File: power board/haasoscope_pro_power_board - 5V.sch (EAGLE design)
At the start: 123 parts, among them CN1 12Vin, IC11 TPS7A7200RGTR, IC12 TPS7A7200RGTR, IC14 TPS7A7200RGTR, IC3 TPS7A7200RGTR, IC5 TPS72325DBVR, IC7 TPS7A7200RGTR, IC9 TPS7A7200RGTR, J1 2p-2.54, J10 2p-2.54, J11 2p-2.54, J12 2p-2.54, J13 2p-2.54, J14 2p-2.54, J15 2p-2.54, J16 8pin, J17 2p-2.54, J18 2p-2.54, J19 2p-2.54, J2 2p-2.54, J20 2p-2.54, J3 2p-2.54, J4 2p-2.54, J5 2p-2.54, J6 2p-2.54, J7 2p-2.54, J8 2p-2.54, J9 2p-2.54

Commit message: add diode
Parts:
- added D6: B340A, SparkFun-DiscreteSemi:DIODE-SCHOTTKY-B340A
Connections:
- net 2V8-: now also D6.A
- net GND: now also D6.C
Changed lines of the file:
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@@
 <part name="R1" library="FlashPCB_Resistors" deviceset="RES-0402" device="" value="3.3k"/>
 <part name="C4" library="Nordic_nRF" library_urn="urn:adsk.eagle:library:169009" deviceset="CAPACITOR" device="_0805_N" package3d_urn="urn:adsk.eagle:package:2593736/1" value="10uF"/>
+<part name="D6" library="SparkFun-DiscreteSemi" library_urn="urn:adsk.eagle:library:514" deviceset="DIODE-SCHOTTKY" device="-B340A" package3d_urn="urn:adsk.eagle:package:38443/1" value="B340A">
+<attribute name="LCSC" value="C64982"/>
+</part>
 </parts>
 <sheets>
@@
 <attribute name="VALUE" x="90.424" y="-44.831" size="1.778" layer="96"/>
 </instance>
+<instance part="D6" gate="G$1" x="215.9" y="-33.02" smashed="yes" rot="R90">
+<attribute name="NAME" x="213.868" y="-35.56" size="1.778" layer="95" font="vector" rot="R90"/>
+<attribute name="VALUE" x="217.932" y="-35.56" size="1.778" layer="96" font="vector" rot="R90" align="top-left"/>
+<attribute name="LCSC" x="215.9" y="-33.02" size="1.778" layer="96" rot="R90" display="off"/>
+</instance>
 </instances>
 <busses>
@@
 <pinref part="C4" gate="C$1" pin="2"/>
 <wire x1="88.9" y1="-45.72" x2="96.52" y2="-45.72" width="0.1524" layer="91"/>
-<wire x1="109.22" y1="-45.72" x2="109.22" y2="-50.8" width="0.1524" layer="91"/>
-<wire x1="109.22" y1="-50.8" x2="99.06" y2="-50.8" width="0.1524" layer="91"/>
+<wire x1="109.22" y1="-45.72" x2="109.22" y2="-55.88" width="0.1524" layer="91"/>
 <junction x="109.22" y="-45.72"/>
-<label x="99.06" y="-50.8" size="1.778" layer="95"/>
-</segment>
-<segment>
 <pinref part="C55" gate="C$1" pin="2"/>
 <pinref part="R20" gate="G$1" pin="P$1"/>
@@
 <wire x1="144.78" y1="-53.34" x2="154.94" y2="-53.34" width="0.1524" layer="91"/>
 <label x="134.62" y="-55.88" size="1.778" layer="95"/>
+<wire x1="109.22" y1="-55.88" x2="129.54" y2="-55.88" width="0.1524" layer="91"/>
+<junction x="129.54" y="-55.88"/>
 </segment>
 <segment>
@@
 <wire x1="175.26" y1="-38.1" x2="185.42" y2="-38.1" width="0.1524" layer="91"/>
 <label x="195.58" y="-38.1" size="1.778" layer="95"/>
+<pinref part="D6" gate="G$1" pin="A"/>
+<wire x1="200.66" y1="-35.56" x2="215.9" y2="-35.56" width="0.1524" layer="91"/>
+<junction x="200.66" y="-35.56"/>
 </segment>
 </net>
@@
 <junction x="96.52" y="7.62"/>
 <pinref part="GND30" gate="1" pin="GND"/>
-</segment>
-<segment>
+<wire x1="109.22" y1="7.62" x2="109.22" y2="-2.54" width="0.1524" layer="91"/>
+<junction x="109.22" y="7.62"/>
 <pinref part="C41" gate="C$1" pin="2"/>
 <pinref part="R13" gate="G$1" pin="P$1"/>
@@
 <wire x1="144.78" y1="0" x2="154.94" y2="0" width="0.1524" layer="91"/>
 <pinref part="GND31" gate="1" pin="GND"/>
+<wire x1="109.22" y1="-2.54" x2="129.54" y2="-2.54" width="0.1524" layer="91"/>
+<junction x="129.54" y="-2.54"/>
 </segment>
 <segment>
@@
 <junction x="185.42" y="-30.48"/>
 <label x="195.58" y="-30.48" size="1.778" layer="95"/>
+<pinref part="D6" gate="G$1" pin="C"/>
+<wire x1="200.66" y1="-30.48" x2="215.9" y2="-30.48" width="0.1524" layer="91"/>
+<junction x="200.66" y="-30.48"/>
 </segment>
 </net>

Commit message: use more standard resistor values
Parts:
- added R2: 15k, FlashPCB_Resistors:RES-0402
- C48: LCSC (none) -> C307331
- R11, R13, R20: value 55k -> 56k
- R16: value 25k -> 10k
- R25: value 37k -> 39k
- R7: value 71k -> 68k
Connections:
- new net N$14: R16.P$1, R2.P$2
- net GND: now also R2.P$1; no longer R16.P$1
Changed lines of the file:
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@@
 <part name="J14" library="Seeed-Connector" library_urn="urn:adsk.eagle:library:478" deviceset="DIP-BLACK-MALE-HEADER-VERT(2P-2.54)" device="" package3d_urn="urn:adsk.eagle:package:33132/1" value="2p-2.54"/>
 <part name="R23" library="FlashPCB_Resistors" deviceset="RES-0402" device="" value="100k"/>
-<part name="R25" library="FlashPCB_Resistors" deviceset="RES-0402" device="" value="37k"/>
+<part name="R25" library="FlashPCB_Resistors" deviceset="RES-0402" device="" value="39k"/>
 <part name="GND23" library="SparkFun-PowerSymbols" library_urn="urn:adsk.eagle:library:530" deviceset="GND" device=""/>
 <part name="PS3" library="LMR33630ADDA" deviceset="LMR33630ADDA" device=""/>
@@
 <part name="J5" library="Seeed-Connector" library_urn="urn:adsk.eagle:library:478" deviceset="DIP-BLACK-MALE-HEADER-VERT(2P-2.54)" device="" package3d_urn="urn:adsk.eagle:package:33132/1" value="2p-2.54"/>
 <part name="R6" library="FlashPCB_Resistors" deviceset="RES-0402" device="" value="100k"/>
-<part name="R7" library="FlashPCB_Resistors" deviceset="RES-0402" device="" value="71k"/>
+<part name="R7" library="FlashPCB_Resistors" deviceset="RES-0402" device="" value="68k"/>
 <part name="GND26" library="SparkFun-PowerSymbols" library_urn="urn:adsk.eagle:library:530" deviceset="GND" device=""/>
 <part name="PS5" library="LMR33630ADDA" deviceset="LMR33630ADDA" device=""/>
@@
 <part name="J7" library="Seeed-Connector" library_urn="urn:adsk.eagle:library:478" deviceset="DIP-BLACK-MALE-HEADER-VERT(2P-2.54)" device="" package3d_urn="urn:adsk.eagle:package:33132/1" value="2p-2.54"/>
 <part name="R8" library="FlashPCB_Resistors" deviceset="RES-0402" device="" value="100k"/>
-<part name="R11" library="FlashPCB_Resistors" deviceset="RES-0402" device="" value="55k"/>
+<part name="R11" library="FlashPCB_Resistors" deviceset="RES-0402" device="" value="56k"/>
 <part name="GND29" library="SparkFun-PowerSymbols" library_urn="urn:adsk.eagle:library:530" deviceset="GND" device=""/>
 <part name="PS6" library="LMR33630ADDA" deviceset="LMR33630ADDA" device=""/>
@@
 <part name="J9" library="Seeed-Connector" library_urn="urn:adsk.eagle:library:478" deviceset="DIP-BLACK-MALE-HEADER-VERT(2P-2.54)" device="" package3d_urn="urn:adsk.eagle:package:33132/1" value="2p-2.54"/>
 <part name="R12" library="FlashPCB_Resistors" deviceset="RES-0402" device="" value="100k"/>
-<part name="R13" library="FlashPCB_Resistors" deviceset="RES-0402" device="" value="55k"/>
+<part name="R13" library="FlashPCB_Resistors" deviceset="RES-0402" device="" value="56k"/>
 <part name="GND32" library="SparkFun-PowerSymbols" library_urn="urn:adsk.eagle:library:530" deviceset="GND" device=""/>
 <part name="PS8" library="LMR33630ADDA" deviceset="LMR33630ADDA" device=""/>
@@
 <part name="J20" library="Seeed-Connector" library_urn="urn:adsk.eagle:library:478" deviceset="DIP-BLACK-MALE-HEADER-VERT(2P-2.54)" device="" package3d_urn="urn:adsk.eagle:package:33132/1" value="2p-2.54"/>
 <part name="R19" library="FlashPCB_Resistors" deviceset="RES-0402" device="" value="100k"/>
-<part name="R20" library="FlashPCB_Resistors" deviceset="RES-0402" device="" value="55k"/>
+<part name="R20" library="FlashPCB_Resistors" deviceset="RES-0402" device="" value="56k"/>
 <part name="PS7" library="LMR33630ADDA" deviceset="LMR33630ADDA" device=""/>
-<part name="C48" library="Nordic_nRF" library_urn="urn:adsk.eagle:library:169009" deviceset="CAPACITOR" device="_0402_N" package3d_urn="urn:adsk.eagle:package:2593732/1" value="0.1uF"/>
+<part name="C48" library="Nordic_nRF" library_urn="urn:adsk.eagle:library:169009" deviceset="CAPACITOR" device="_0402_N" package3d_urn="urn:adsk.eagle:package:2593732/1" value="0.1uF">
+<attribute name="LCSC" value="
+C307331"/>
+</part>
 <part name="GND33" library="SparkFun-PowerSymbols" library_urn="urn:adsk.eagle:library:530" deviceset="GND" device=""/>
 <part name="C49" library="Nordic_nRF" library_urn="urn:adsk.eagle:library:169009" deviceset="CAPACITOR" device="_0402_N" package3d_urn="urn:adsk.eagle:package:2593732/1" value="0.1uF"/>
@@
 <part name="J11" library="Seeed-Connector" library_urn="urn:adsk.eagle:library:478" deviceset="DIP-BLACK-MALE-HEADER-VERT(2P-2.54)" device="" package3d_urn="urn:adsk.eagle:package:33132/1" value="2p-2.54"/>
 <part name="R15" library="FlashPCB_Resistors" deviceset="RES-0402" device="" value="100k"/>
-<part name="R16" library="FlashPCB_Resistors" deviceset="RES-0402" device="" value="25k"/>
+<part name="R16" library="FlashPCB_Resistors" deviceset="RES-0402" device="" value="10k"/>
 <part name="GND35" library="SparkFun-PowerSymbols" library_urn="urn:adsk.eagle:library:530" deviceset="GND" device=""/>
 <part name="GND2" library="SparkFun-PowerSymbols" library_urn="urn:adsk.eagle:library:530" deviceset="GND" device=""/>
@@
 <attribute name="LCSC" value="C64982"/>
 </part>
+<part name="R2" library="FlashPCB_Resistors" deviceset="RES-0402" device="" value="15k"/>
 </parts>
 <sheets>
@@
 <attribute name="NAME" x="98.044" y="-85.979" size="1.778" layer="95"/>
 <attribute name="VALUE" x="98.044" y="-90.551" size="1.778" layer="96"/>
+<attribute name="LCSC" x="96.52" y="-88.9" size="1.778" layer="96" display="off"/>
 </instance>
 <instance part="GND33" gate="1" x="96.52" y="-96.52" smashed="yes">
@@
 <attribute name="VALUE" x="217.932" y="-35.56" size="1.778" layer="96" font="vector" rot="R90" align="top-left"/>
 <attribute name="LCSC" x="215.9" y="-33.02" size="1.778" layer="96" rot="R90" display="off"/>
+</instance>
+<instance part="R2" gate="G$1" x="170.18" y="-106.68" smashed="yes" rot="R90">
+<attribute name="NAME" x="168.6814" y="-110.49" size="1.778" layer="95" rot="R90"/>
+<attribute name="VALUE" x="173.482" y="-110.49" size="1.778" layer="96" rot="R90"/>
 </instance>
 </instances>
@@
 <segment>
 <pinref part="C50" gate="C$1" pin="2"/>
-<pinref part="R16" gate="G$1" pin="P$1"/>
-<wire x1="154.94" y1="-101.6" x2="170.18" y2="-101.6" width="0.1524" layer="91"/>
 <junction x="154.94" y="-101.6"/>
 <pinref part="PS7" gate="G$1" pin="EP"/>
@@
 <wire x1="144.78" y1="-101.6" x2="154.94" y2="-101.6" width="0.1524" layer="91"/>
 <pinref part="GND34" gate="1" pin="GND"/>
+<wire x1="154.94" y1="-101.6" x2="162.56" y2="-101.6" width="0.1524" layer="91"/>
+<wire x1="162.56" y1="-101.6" x2="162.56" y2="-111.76" width="0.1524" layer="91"/>
+<pinref part="R2" gate="G$1" pin="P$1"/>
+<wire x1="162.56" y1="-111.76" x2="170.18" y2="-111.76" width="0.1524" layer="91"/>
 </segment>
 <segment>
@@
 </segment>
 </net>
+<net name="N$14" class="0">
+<segment>
+<pinref part="R16" gate="G$1" pin="P$1"/>
+<pinref part="R2" gate="G$1" pin="P$2"/>
+</segment>
+</net>

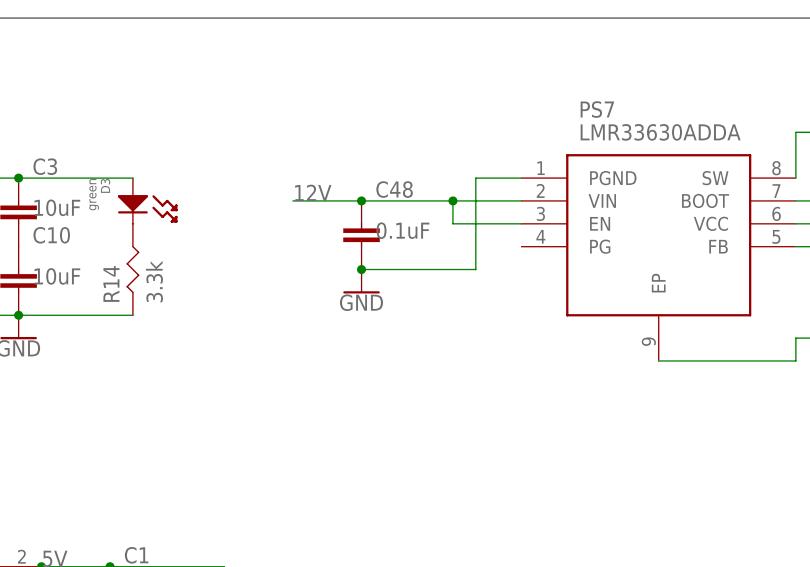
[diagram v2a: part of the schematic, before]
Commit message: add another 12V cap
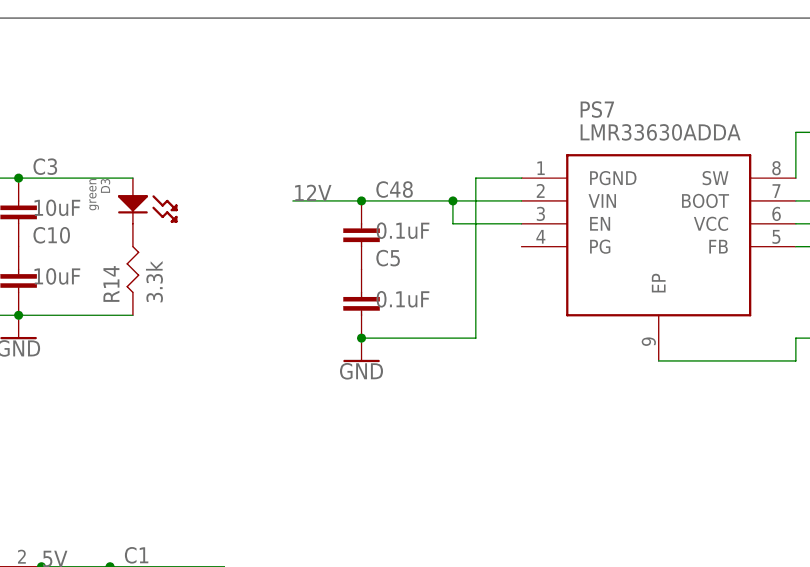
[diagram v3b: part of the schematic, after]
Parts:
- added C5: 0.1uF, Nordic_nRF:CAPACITOR_0402_N
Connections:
- new net N$40: C48.2, C5.1
- net GND: now also C5.2; no longer C48.2
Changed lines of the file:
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@@
 C307331"/>
 </part>
-<part name="GND33" library="SparkFun-PowerSymbols" library_urn="urn:adsk.eagle:library:530" deviceset="GND" device=""/>
 <part name="C49" library="Nordic_nRF" library_urn="urn:adsk.eagle:library:169009" deviceset="CAPACITOR" device="_0402_N" package3d_urn="urn:adsk.eagle:package:2593732/1" value="0.1uF"/>
 <part name="C50" library="Nordic_nRF" library_urn="urn:adsk.eagle:library:169009" deviceset="CAPACITOR" device="_0402_N" package3d_urn="urn:adsk.eagle:package:2593732/1" value="1uF"/>
@@
 </part>
 <part name="R2" library="FlashPCB_Resistors" deviceset="RES-0402" device="" value="15k"/>
+<part name="C5" library="Nordic_nRF" library_urn="urn:adsk.eagle:library:169009" deviceset="CAPACITOR" device="_0402_N" package3d_urn="urn:adsk.eagle:package:2593732/1" value="0.1uF">
+<attribute name="LCSC" value="
+C307331"/>
+</part>
+<part name="GND3" library="SparkFun-PowerSymbols" library_urn="urn:adsk.eagle:library:530" deviceset="GND" device=""/>
 </parts>
 <sheets>
@@
 <attribute name="LCSC" x="96.52" y="-88.9" size="1.778" layer="96" display="off"/>
 </instance>
-<instance part="GND33" gate="1" x="96.52" y="-96.52" smashed="yes">
-<attribute name="VALUE" x="96.52" y="-96.774" size="1.778" layer="96" align="top-center"/>
-</instance>
 <instance part="C49" gate="C$1" x="154.94" y="-81.28" smashed="yes">
 <attribute name="NAME" x="156.464" y="-80.899" size="1.778" layer="95"/>
@@
 <attribute name="NAME" x="168.6814" y="-110.49" size="1.778" layer="95" rot="R90"/>
 <attribute name="VALUE" x="173.482" y="-110.49" size="1.778" layer="96" rot="R90"/>
+</instance>
+<instance part="C5" gate="C$1" x="96.52" y="-96.52" smashed="yes">
+<attribute name="NAME" x="98.044" y="-93.599" size="1.778" layer="95"/>
+<attribute name="VALUE" x="98.044" y="-98.171" size="1.778" layer="96"/>
+<attribute name="LCSC" x="96.52" y="-96.52" size="1.778" layer="96" display="off"/>
+</instance>
+<instance part="GND3" gate="1" x="96.52" y="-104.14" smashed="yes">
+<attribute name="VALUE" x="96.52" y="-104.394" size="1.778" layer="96" align="top-center"/>
 </instance>
 </instances>
@@
 </segment>
 <segment>
-<pinref part="C48" gate="C$1" pin="2"/>
-<pinref part="PS7" gate="G$1" pin="PGND"/>
-<wire x1="114.3" y1="-83.82" x2="109.22" y2="-83.82" width="0.1524" layer="91"/>
-<wire x1="109.22" y1="-83.82" x2="109.22" y2="-93.98" width="0.1524" layer="91"/>
-<wire x1="109.22" y1="-93.98" x2="96.52" y2="-93.98" width="0.1524" layer="91"/>
-<junction x="96.52" y="-93.98"/>
-<pinref part="GND33" gate="1" pin="GND"/>
-</segment>
-<segment>
 <pinref part="C50" gate="C$1" pin="2"/>
 <junction x="154.94" y="-101.6"/>
@@
 <wire x1="200.66" y1="-30.48" x2="215.9" y2="-30.48" width="0.1524" layer="91"/>
 <junction x="200.66" y="-30.48"/>
+</segment>
+<segment>
+<pinref part="C5" gate="C$1" pin="2"/>
+<pinref part="GND3" gate="1" pin="GND"/>
+<wire x1="96.52" y1="-101.6" x2="109.22" y2="-101.6" width="0.1524" layer="91"/>
+<junction x="96.52" y="-101.6"/>
+<pinref part="PS7" gate="G$1" pin="PGND"/>
+<wire x1="114.3" y1="-83.82" x2="109.22" y2="-83.82" width="0.1524" layer="91"/>
+<wire x1="109.22" y1="-83.82" x2="109.22" y2="-101.6" width="0.1524" layer="91"/>
 </segment>
 </net>
@@
 </segment>
 </net>
+<net name="N$40" class="0">
+<segment>
+<pinref part="C48" gate="C$1" pin="2"/>
+<pinref part="C5" gate="C$1" pin="1"/>
+</segment>
+</net>

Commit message: add another 12V cap
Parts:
- C48, C5: LCSC C307331 -> C307331
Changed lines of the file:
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@@
 <part name="PS7" library="LMR33630ADDA" deviceset="LMR33630ADDA" device=""/>
 <part name="C48" library="Nordic_nRF" library_urn="urn:adsk.eagle:library:169009" deviceset="CAPACITOR" device="_0402_N" package3d_urn="urn:adsk.eagle:package:2593732/1" value="0.1uF">
-<attribute name="LCSC" value="
-C307331"/>
+<attribute name="LCSC" value="C307331"/>
 </part>
 <part name="C49" library="Nordic_nRF" library_urn="urn:adsk.eagle:library:169009" deviceset="CAPACITOR" device="_0402_N" package3d_urn="urn:adsk.eagle:package:2593732/1" value="0.1uF"/>
@@
 <part name="R2" library="FlashPCB_Resistors" deviceset="RES-0402" device="" value="15k"/>
 <part name="C5" library="Nordic_nRF" library_urn="urn:adsk.eagle:library:169009" deviceset="CAPACITOR" device="_0402_N" package3d_urn="urn:adsk.eagle:package:2593732/1" value="0.1uF">
-<attribute name="LCSC" value="
-C307331"/>
+<attribute name="LCSC" value="C307331"/>
 </part>
 <part name="GND3" library="SparkFun-PowerSymbols" library_urn="urn:adsk.eagle:library:530" deviceset="GND" device=""/>

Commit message: use 4x22uF 0805 caps instead of 100uF tants
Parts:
- removed C45, C56: 100uF, SparkFun-Passives:CAP_POLSMD
- added C58, C6, C61, C62, C63, C64, C65, C66, C67, C68, C69, C70, C71, C72, C77, C78, C79, C80, C81, C82, C83, C84: 22uF, Nordic_nRF:CAPACITOR_0805_N
- C15, C24, C33, C42, C51: value 100uF -> 22uF; device SparkFun-Passives:CAP_POLSMD -> Nordic_nRF:CAPACITOR_0805_N; LCSC C7230 -> (none)
- C5: value 0.1uF -> 22uF; device Nordic_nRF:CAPACITOR_0402_N -> Nordic_nRF:CAPACITOR_0805_N; LCSC C307331 -> (none)
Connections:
- removed net N$2: C1.2, C2.1
- removed net N$40: C48.2, C5.1
- net 1V5: now also C65.1, C66.1, C67.1, C68.1; no longer C15.+
- net 2V4: now also C77.1, C78.1, C79.1, C80.1; no longer C24.+
- net 2V8+: now also C61.1, C62.1, C63.1, C64.1; no longer C42.+
- net 2V8-: now also C15.2, C24.2, C33.2, C42.2; no longer C56.-
- net 2V8D: now also C69.1, C70.1, C71.1, C72.1; no longer C33.+
- net 3V7: now also C81.1, C82.1, C83.1, C84.1; no longer C45.+
- net 5V: now also C2.1, C5.1, C51.1, C58.1, C6.1; no longer C51.+
- net GND: now also C1.2, C15.1, C24.1, C33.1, C42.1, C48.2, C51.2, C58.2, C6.2, C61.2, C62.2, C63.2, C64.2, C65.2, C66.2, C67.2, C68.2, C69.2, C70.2, C71.2, C72.2, C77.2, C78.2, C79.2, C80.2, C81.2, C82.2, C83.2, C84.2; no longer C15.-, C24.-, C33.-, C42.-, C45.-, C51.-, C56.+
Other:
- moved on the sheet: C2, C5, D1, R1

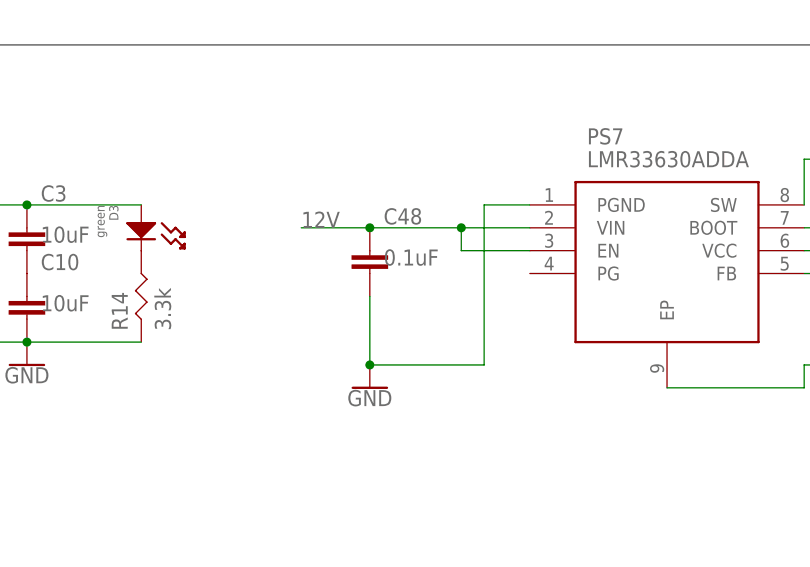
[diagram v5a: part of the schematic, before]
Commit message: add another 12V cap
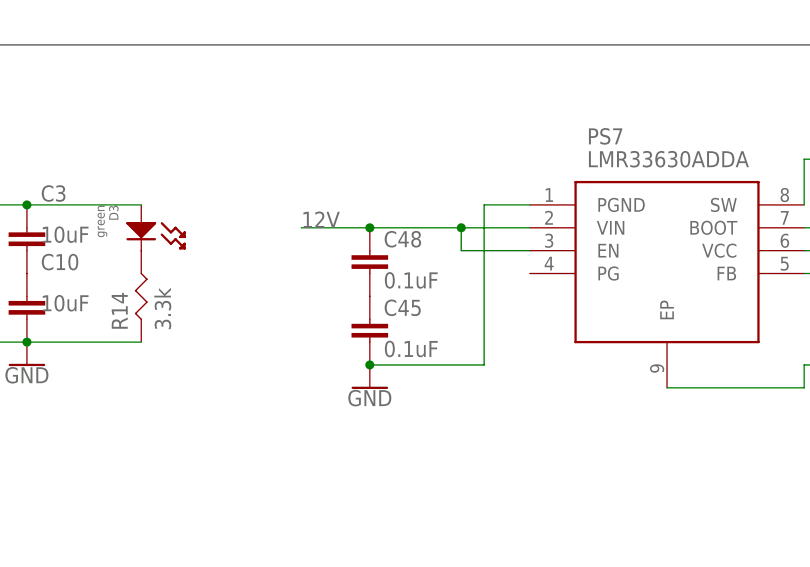
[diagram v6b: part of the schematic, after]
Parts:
- added C45: 0.1uF, Nordic_nRF:CAPACITOR_0402_N
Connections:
- new net N$2: C45.1, C48.2
- net GND: now also C45.2; no longer C48.2
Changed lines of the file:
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@@
 <part name="C83" library="Nordic_nRF" library_urn="urn:adsk.eagle:library:169009" deviceset="CAPACITOR" device="_0805_N" package3d_urn="urn:adsk.eagle:package:2593736/1" value="22uF"/>
 <part name="C84" library="Nordic_nRF" library_urn="urn:adsk.eagle:library:169009" deviceset="CAPACITOR" device="_0805_N" package3d_urn="urn:adsk.eagle:package:2593736/1" value="22uF"/>
+<part name="C45" library="Nordic_nRF" library_urn="urn:adsk.eagle:library:169009" deviceset="CAPACITOR" device="_0402_N" package3d_urn="urn:adsk.eagle:package:2593732/1" value="0.1uF">
+<attribute name="LCSC" value="C307331"/>
+</part>
 </parts>
 <sheets>
@@
 </instance>
 <instance part="C48" gate="C$1" x="96.52" y="-88.9" smashed="yes">
-<attribute name="NAME" x="98.044" y="-85.979" size="1.778" layer="95"/>
-<attribute name="VALUE" x="98.044" y="-90.551" size="1.778" layer="96"/>
+<attribute name="NAME" x="98.044" y="-88.519" size="1.778" layer="95"/>
+<attribute name="VALUE" x="98.044" y="-93.091" size="1.778" layer="96"/>
 <attribute name="LCSC" x="96.52" y="-88.9" size="1.778" layer="96" display="off"/>
 </instance>
@@
 <attribute name="NAME" x="197.104" y="335.661" size="1.778" layer="95"/>
 <attribute name="VALUE" x="197.104" y="331.089" size="1.778" layer="96"/>
+</instance>
+<instance part="C45" gate="C$1" x="96.52" y="-96.52" smashed="yes">
+<attribute name="NAME" x="98.044" y="-96.139" size="1.778" layer="95"/>
+<attribute name="VALUE" x="98.044" y="-100.711" size="1.778" layer="96"/>
+<attribute name="LCSC" x="96.52" y="-96.52" size="1.778" layer="96" display="off"/>
 </instance>
 </instances>
@@
 <wire x1="114.3" y1="-83.82" x2="109.22" y2="-83.82" width="0.1524" layer="91"/>
 <wire x1="109.22" y1="-83.82" x2="109.22" y2="-101.6" width="0.1524" layer="91"/>
-<pinref part="C48" gate="C$1" pin="2"/>
-<wire x1="96.52" y1="-93.98" x2="96.52" y2="-101.6" width="0.1524" layer="91"/>
+<pinref part="C45" gate="C$1" pin="2"/>
 <junction x="96.52" y="-101.6"/>
 </segment>
@@
 </segment>
 </net>
+<net name="N$2" class="0">
+<segment>
+<pinref part="C48" gate="C$1" pin="2"/>
+<pinref part="C45" gate="C$1" pin="1"/>
+</segment>
+</net>
